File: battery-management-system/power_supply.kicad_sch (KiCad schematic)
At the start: 49 parts, among them J14 -5V, J24 3V3, J25 5V, J26 18V, J28 9V4, U1 L6982C33DR, U12 ICL7660, U15 ICL7660, U16 ICL7660, U2 L6982C33DR

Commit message: improve layout
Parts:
- renumbered C36 to C1, C5 to C10, C38 to C11, C39 to C12, C7 to C13, C8 to C14, C28 to C2, C1 to C3, C2 to C4, C29 to C5, C37 to C6, C3 to C7, C4 to C8, C6 to C9, D5 to D10, D23 to D11, D24 to D12, D25 to D13, D20 to D14, D21 to D15, D22 to D16, D15 to D7, D3 to D8, D4 to D9, J28 to J10, J25 to J11, J26 to J12, J24 to J13, J14 to J9, R5 to R10, R7 to R11, R8 to R12, R9 to R13, R10 to R14, R11 to R15, R52 to R16, R44 to R17, R51 to R18, R43 to R6, R45 to R7, R4 to R8, R6 to R9, U15 to U1, U12 to U2, U1 to U3, U2 to U4, U16 to U5

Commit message: simplify cell measurement
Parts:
- removed C2, C5: 10uF, benediktibk:C_1210_3225Metric_Pad1.33x2.70mm_HandSolder, symbol benediktibk:C_10uF_SMD_1210_50V_20%
- removed J10: 9V4, benediktibk:PinHeader_1x03_P2.54mm_Vertical, symbol benediktibk:Conn_01x03
- removed J9: -5V, benediktibk:PinHeader_1x03_P2.54mm_Vertical, symbol benediktibk:Conn_01x03
- removed R6, R7: 2mOhm, benediktibk:R_2512_6332Metric_Pad1.40x3.35mm_HandSolder, symbol benediktibk:R_2mOhm_SMD_2512_5W_1%
- removed U2: ICL7660, benediktibk:SOIC-8_3.9x4.9mm_P1.27mm, symbol benediktibk:ICL7660
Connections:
- net 9V4: now also D12.2 (A), U5.8 (V+)
- no-connect marks 11 -> 8

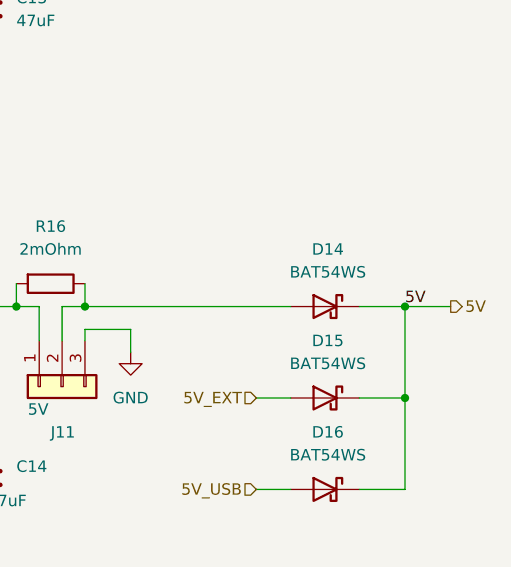
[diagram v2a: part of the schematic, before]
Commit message: fix electrical rule check errors
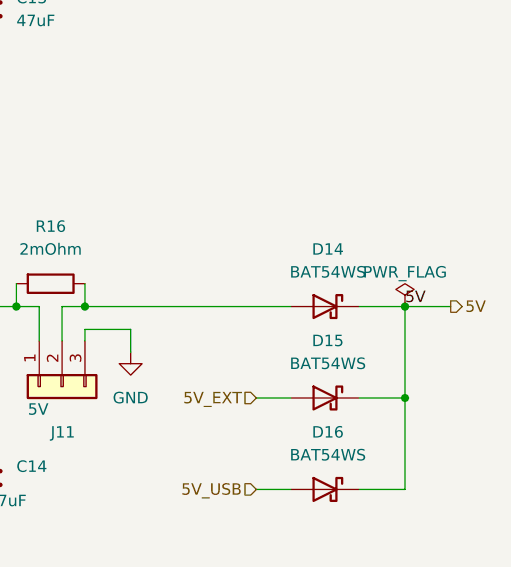
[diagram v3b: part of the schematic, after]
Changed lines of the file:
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@@
+    )
+  )
+  (symbol (lib_id "power:PWR_FLAG") (at 219.71 72.39 0) (unit 1)
+    (in_bom yes) (on_board yes) (dnp no)
+    (property "Reference" "#FLG09" (at 219.71 70.485 0)
+      (effects (font (size 1.27 1.27)) hide)
+    )
+    (property "Value" "PWR_FLAG" (at 219.71 68.58 0)
+      (effects (font (size 1.27 1.27)))
+    )
+    (property "Footprint" "" (at 219.71 72.39 0)
+      (effects (font (size 1.27 1.27)) hide)
+    )
+    (property "Datasheet" "~" (at 219.71 72.39 0)
+      (effects (font (size 1.27 1.27)) hide)
+    )
+    (pin "1")
+    (instances
+      (project "battery-management-system"
+        (path "/5272f0ff-3069-41a9-bca2-80beede8b4b2/b1377397-46a1-4623-af59-88e4e694ca35"
+          (reference "#FLG09") (unit 1)
+        )
+      )
     )
   )

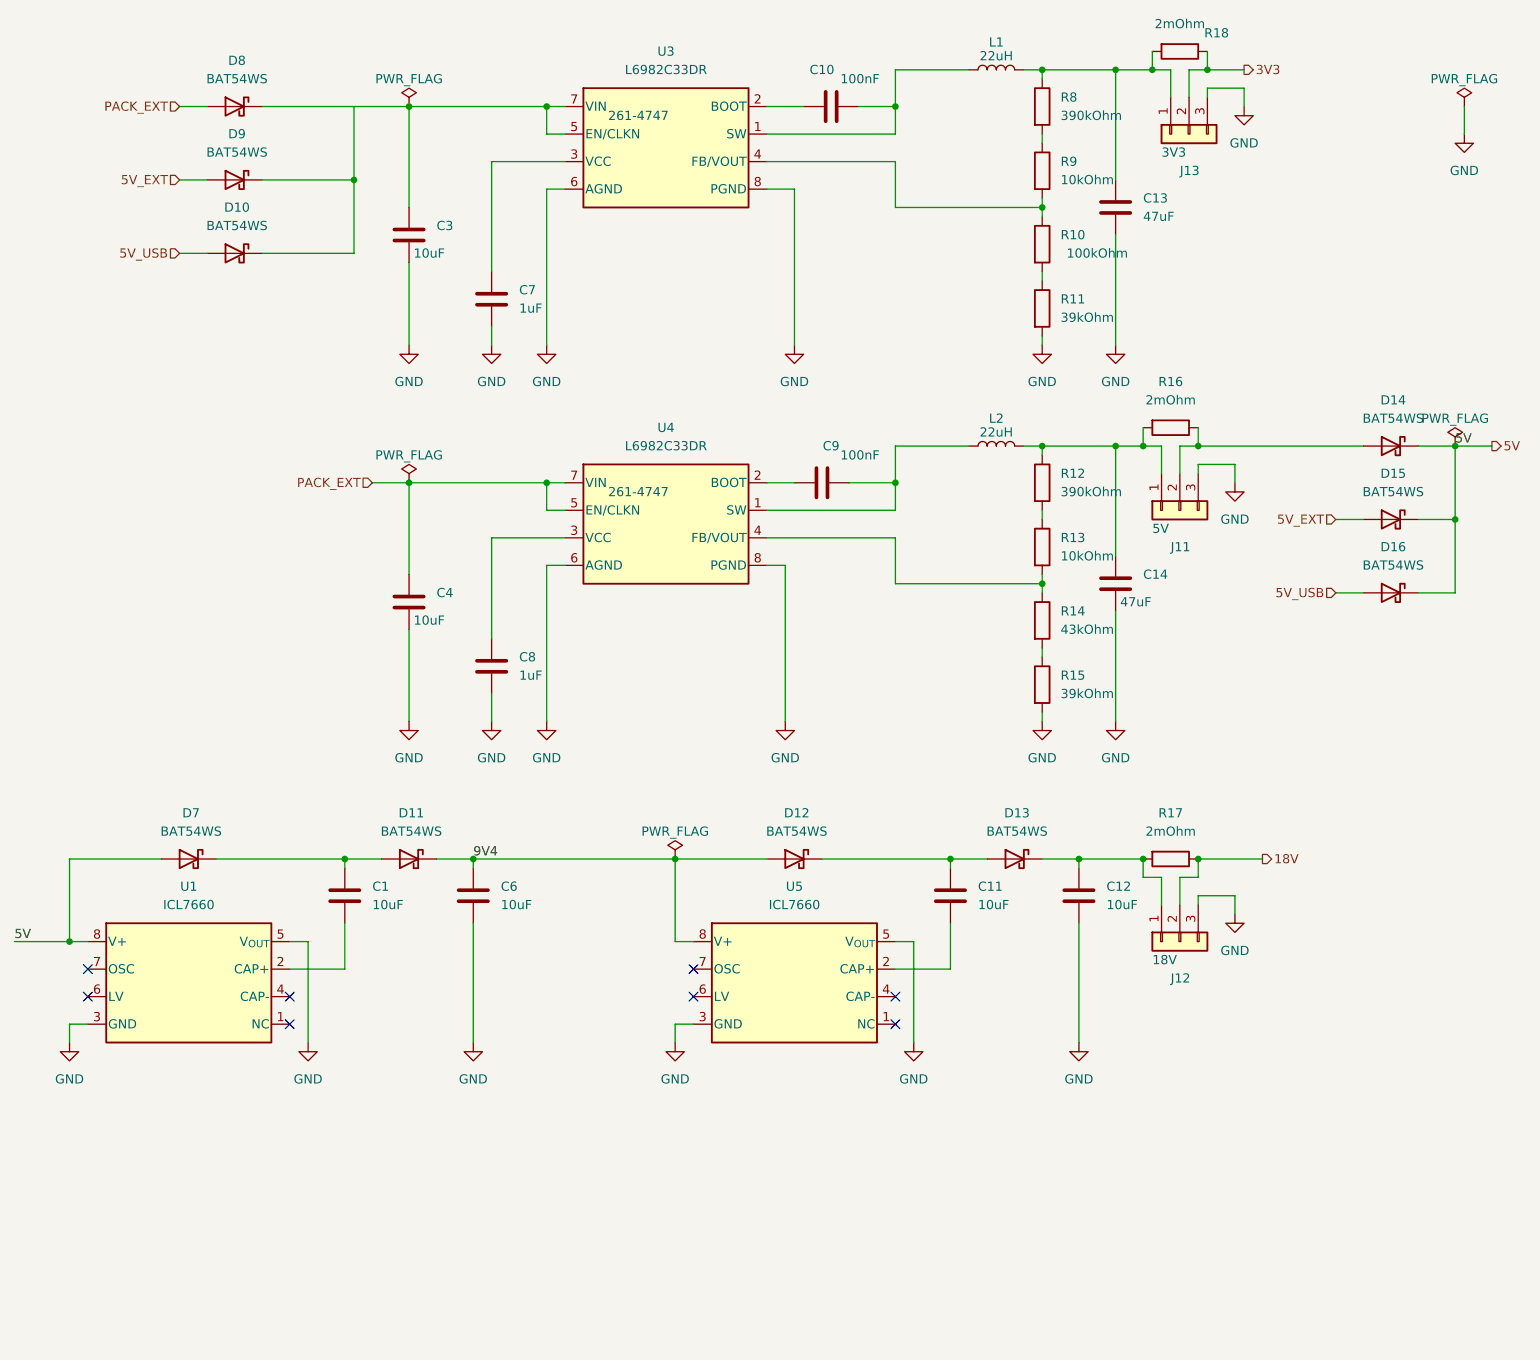
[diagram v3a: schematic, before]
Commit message: add enable input for cell measurement
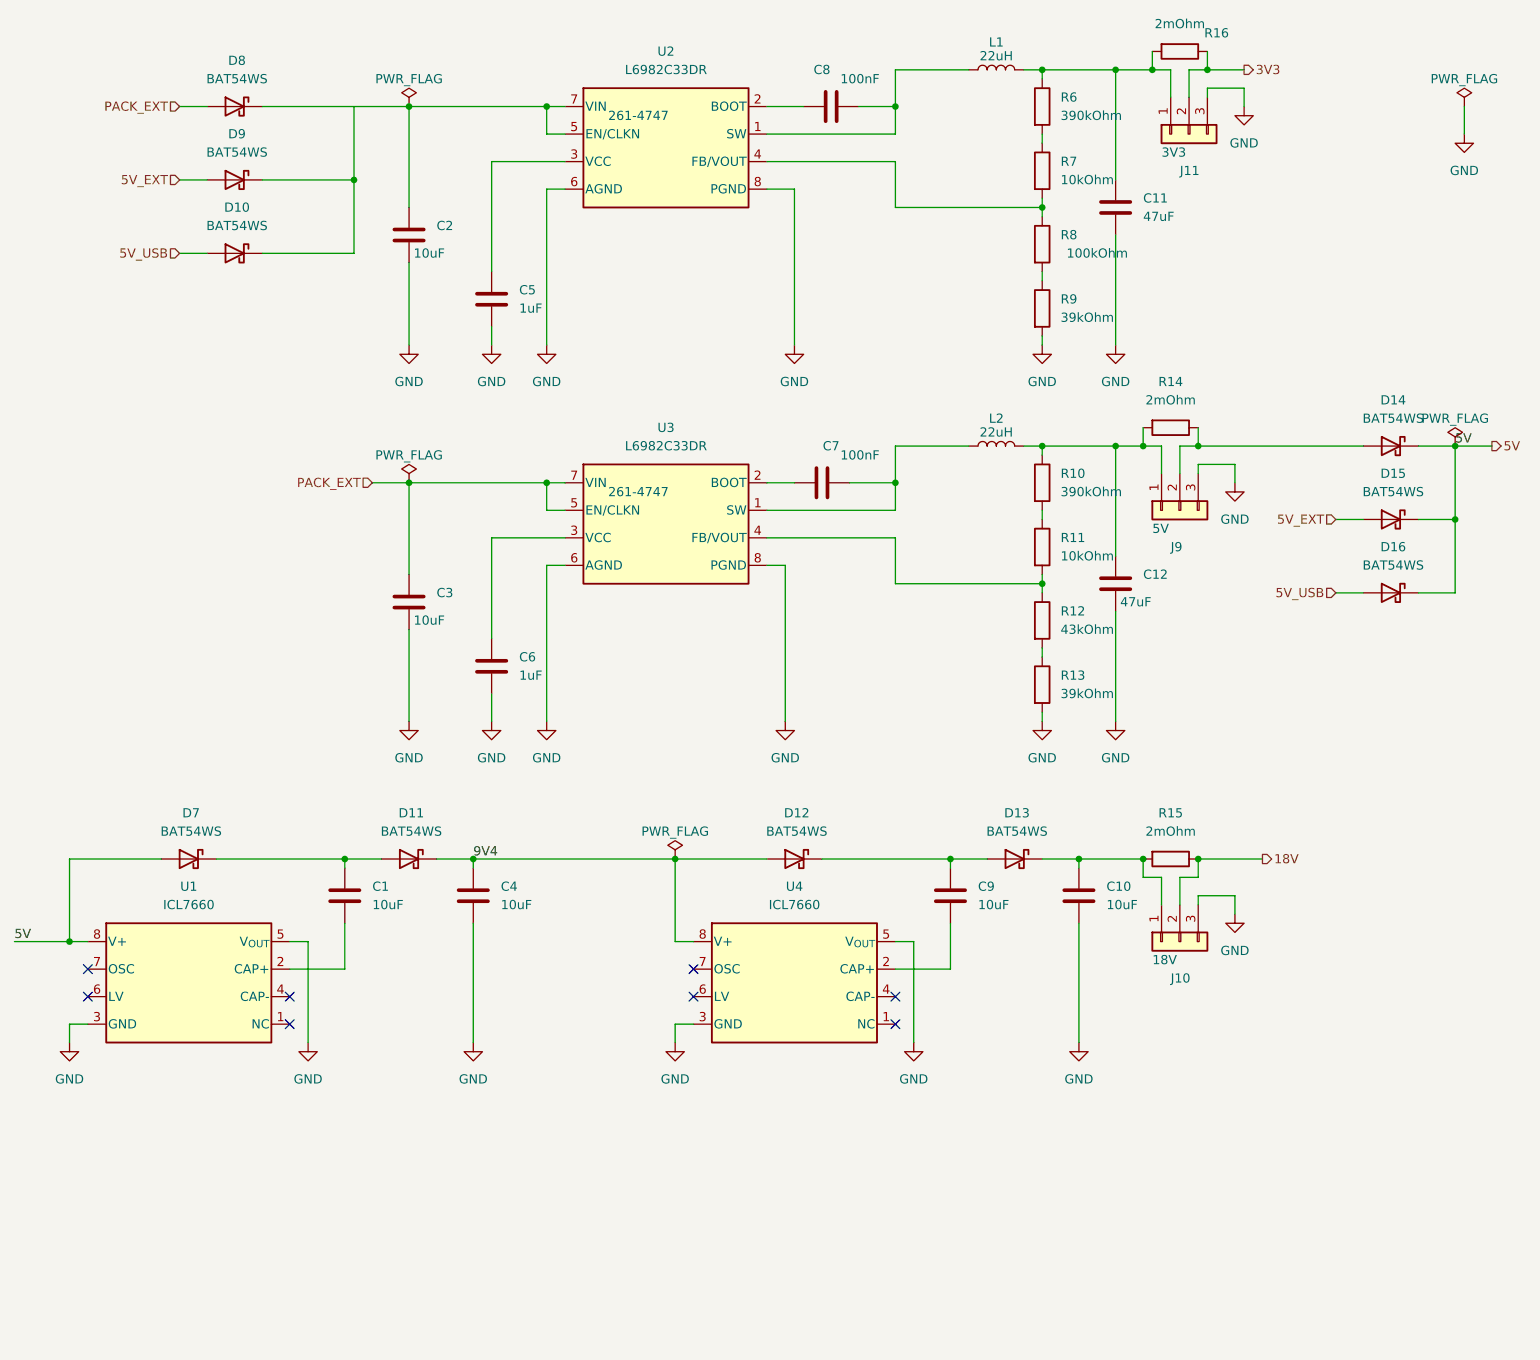
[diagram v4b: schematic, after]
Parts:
- renumbered C12 to C10, C13 to C11, C14 to C12, C3 to C2, C4 to C3, C6 to C4, C7 to C5, C8 to C6, C9 to C7, C10 to C8, C11 to C9, J12 to J10, J13 to J11, J11 to J9, R12 to R10, R13 to R11, R14 to R12, R15 to R13, R16 to R14, R17 to R15, R18 to R16, R8 to R6, R9 to R7, R10 to R8, R11 to R9, U3 to U2, U4 to U3, U5 to U4

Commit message: finish layout of cell measurement
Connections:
- net at C2.1, D8.1 (K), U2.5 (EN/CLKN)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: now also D10.1 (K), D9.1 (K)
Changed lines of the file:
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@@
   (junction (at 185.42 20.32) (diameter 0) (color 0 0 0 0)
+  )
+  (junction (at 67.31 25.4) (diameter 0) (color 0 0 0 0)
   )
   (junction (at 111.76 129.54) (diameter 0) (color 0 0 0 0)
@@
     (stroke (width 0) (type default))
   )
+  (wire (pts (xy 67.31 25.4) (xy 74.93 25.4))
+    (stroke (width 0) (type default))
+  )
   (wire (pts (xy 96.52 88.9) (xy 93.98 88.9))
     (stroke (width 0) (type default))
@@
     (stroke (width 0) (type default))
   )
-  (wire (pts (xy 54.61 25.4) (xy 74.93 25.4))
-    (stroke (width 0) (type default))
-  )
   (wire (pts (xy 74.93 97.79) (xy 74.93 110.49))
     (stroke (width 0) (type default))
@@
     (stroke (width 0) (type default))
   )
+  (wire (pts (xy 54.61 25.4) (xy 67.31 25.4))
+    (stroke (width 0) (type default))
+  )
